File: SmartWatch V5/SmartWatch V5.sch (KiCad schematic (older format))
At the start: 61 parts, among them J1 10118192-0001LF, J10 TestPad, J2 , J8 TestPad, J9 TestPad, Q1 FDN340P, Q2 MMBT3904, Q3 MMBT3904, Q4 FDN028N20, Q5 FDN028N20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

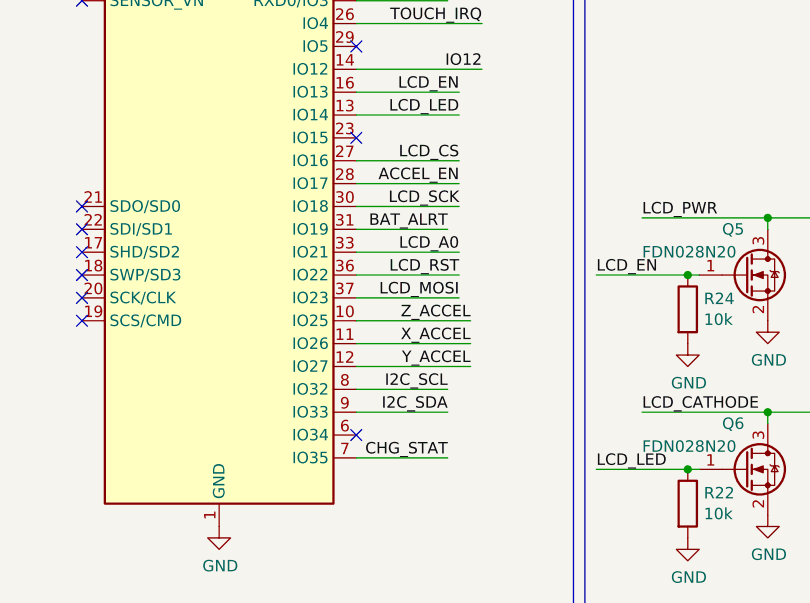
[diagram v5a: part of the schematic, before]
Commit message: Changed ACCEL_EN to IO34
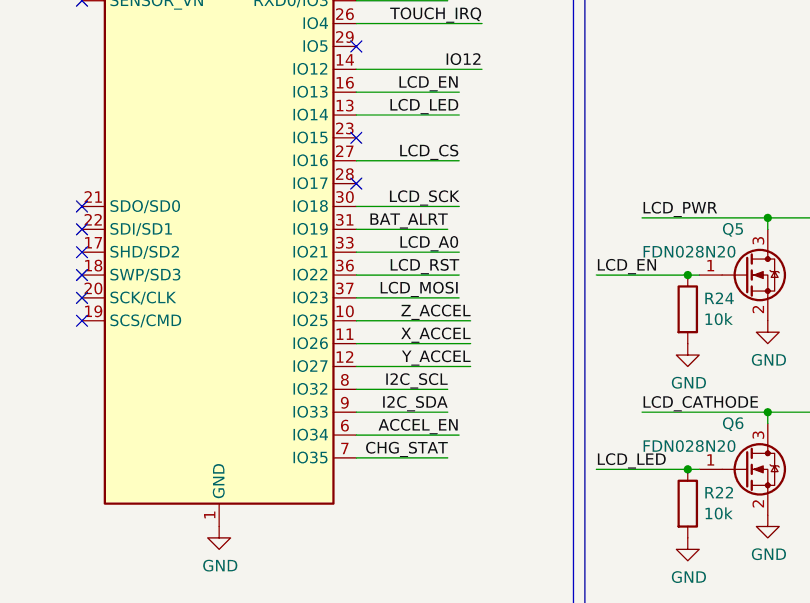
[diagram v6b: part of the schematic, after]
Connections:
- net ACCEL_EN: now also U6.6 (IO34); no longer U6.28 (IO17)
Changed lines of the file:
@@
 LCD_CS
-Wire Wire Line
-	7950 3150 8450 3150
 Wire Wire Line
 	7950 3250 8450 3250
@@
 	1    0    0    -1
 $EndComp
-Text Label 8450 3150 2    50   ~ 0
-Z_ACCEL
 Text Label 8450 3250 2    50   ~ 0
 X_ACCEL
@@
 Wire Wire Line
 	4300 2550 4650 2550
-Text Label 8400 2550 2    50   ~ 0
-ACCEL_EN
-Wire Wire Line
-	7950 2550 8400 2550
 $Comp
 L RF_Module:ESP32-WROOM-32 U6
@@
 Text Label 8350 2750 2    50   ~ 0
 BAT_ALRT
-NoConn ~ 7950 3650
 $Comp
 L power:+3.3V #PWR0129
@@
 Wire Wire Line
 	3150 1300 3600 1300
+Text Label 8450 3150 2    50   ~ 0
+Z_ACCEL
+Wire Wire Line
+	7950 3150 8450 3150
+Text Label 8400 3650 2    50   ~ 0
+ACCEL_EN
+Wire Wire Line
+	7950 3650 8400 3650
+NoConn ~ 7950 2550
 $EndSCHEMATC

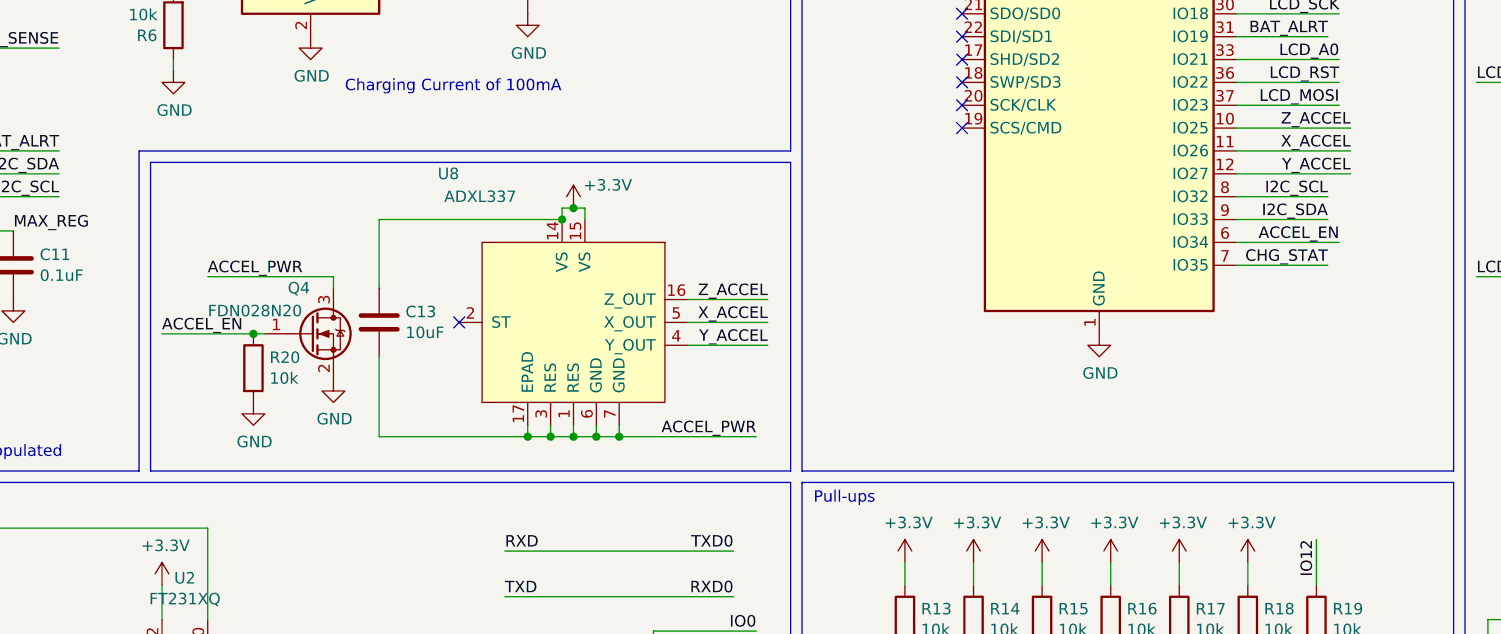
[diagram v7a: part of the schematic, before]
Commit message: Changed V5 schematic to remove enable mosfet from accelerometer
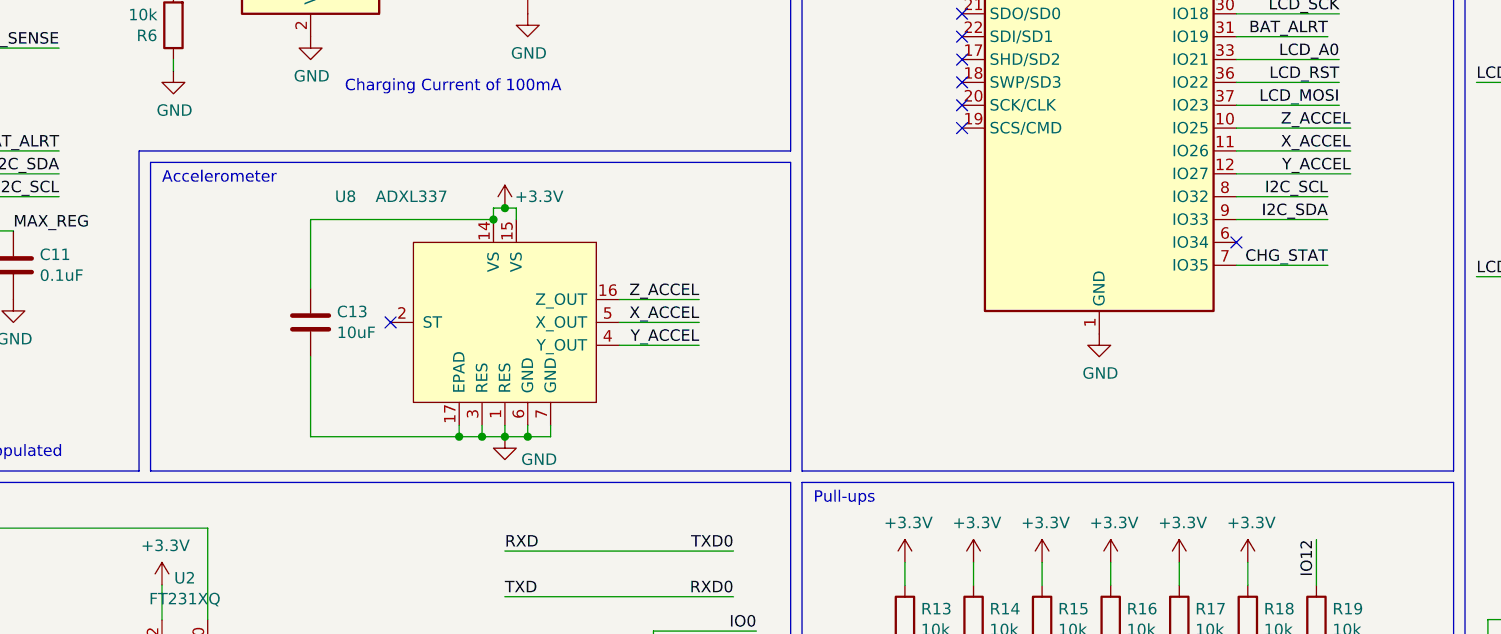
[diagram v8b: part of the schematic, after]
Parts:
- removed Q4: FDN028N20, Package_TO_SOT_SMD:SOT-23, symbol Device:Q_NMOS_GSD
- removed R20: 10k, Resistor_SMD:R_0603_1608Metric, symbol Device:R
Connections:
- net ACCEL_PWR is gone; now on net GND: C13.2, U8.1 (RES), U8.17 (EPAD), U8.3 (RES), U8.6 (GND), U8.7 (GND)
- net ACCEL_EN: no longer names the net of U6.6 (IO34)
- no-connect marks 28 -> 29
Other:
- note added: "Accelerometer\n"
- moved on the sheet: C13, U8
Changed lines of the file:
@@
 L power:+3.3V #PWR0133
 U 1 1 5F663FDD
-P 5050 3500
-F 0 "#PWR0133" H 5050 3350 50  0001 C CNN
-F 1 "+3.3V" H 5200 3600 50  0000 C CNN
-F 2 "" H 5050 3500 50  0001 C CNN
-F 3 "" H 5050 3500 50  0001 C CNN
-	1    5050 3500
-	1    0    0    -1
-$EndComp
-Wire Wire Line
-	5000 3550 5000 3500
-Wire Wire Line
-	5000 3500 5050 3500
-Wire Wire Line
-	5100 3500 5100 3550
-Connection ~ 5050 3500
-Wire Wire Line
-	5050 3500 5100 3500
+P 4750 3500
+F 0 "#PWR0133" H 4750 3350 50  0001 C CNN
+F 1 "+3.3V" H 4900 3550 50  0000 C CNN
+F 2 "" H 4750 3500 50  0001 C CNN
+F 3 "" H 4750 3500 50  0001 C CNN
+	1    4750 3500
+	1    0    0    -1
+$EndComp
+Wire Wire Line
+	4700 3550 4700 3500
+Wire Wire Line
+	4700 3500 4750 3500
+Wire Wire Line
+	4800 3500 4800 3550
+Connection ~ 4750 3500
+Wire Wire Line
+	4750 3500 4800 3500
+Wire Wire Line
+	4550 4450 4550 4500
+Wire Wire Line
+	4550 4500 4650 4500
+Wire Wire Line
+	4950 4500 4950 4450
 Wire Wire Line
 	4850 4450 4850 4500
+Connection ~ 4850 4500
 Wire Wire Line
 	4850 4500 4950 4500
 Wire Wire Line
-	5250 4500 5250 4450
-Wire Wire Line
-	5150 4450 5150 4500
-Connection ~ 5150 4500
-Wire Wire Line
-	5150 4500 5250 4500
-Wire Wire Line
-	5050 4450 5050 4500
-Connection ~ 5050 4500
-Wire Wire Line
-	5050 4500 5150 4500
-Wire Wire Line
-	4950 4450 4950 4500
-Connection ~ 4950 4500
-Wire Wire Line
-	4950 4500 5050 4500
-NoConn ~ 4550 4000
-Text Label 5900 3900 2    50   ~ 0
+	4750 4450 4750 4500
+Connection ~ 4750 4500
+Wire Wire Line
+	4750 4500 4850 4500
+Wire Wire Line
+	4650 4450 4650 4500
+Connection ~ 4650 4500
+Wire Wire Line
+	4650 4500 4750 4500
+NoConn ~ 4250 4000
+Text Label 5600 3900 2    50   ~ 0
 Z_ACCEL
-Text Label 5900 4000 2    50   ~ 0
+Text Label 5600 4000 2    50   ~ 0
 X_ACCEL
-Text Label 5900 4100 2    50   ~ 0
+Text Label 5600 4100 2    50   ~ 0
 Y_ACCEL
 Wire Wire Line
-	5900 3900 5550 3900
-Wire Wire Line
-	5900 4000 5550 4000
-Wire Wire Line
-	5900 4100 5550 4100
+	5600 3900 5250 3900
+Wire Wire Line
+	5600 4000 5250 4000
+Wire Wire Line
+	5600 4100 5250 4100
 $Comp
 L CustomParts:ADXL337 U8
 U 1 1 5F663623
-P 5050 4000
-F 0 "U8" H 4550 4650 50  0000 R CNN
-F 1 "ADXL337" H 4800 4550 50  0000 R CNN
-F 2 "CustomFootprints:ADXL337BCPZ-RL" H 4600 4450 50  0001 C CNN
-F 3 "https://www.analog.com/media/en/technical-documentation/data-sheets/ADXL337.pdf" H 4600 4450 50  0001 C CNN
-F 4 "ADXL337BCPZ-RLCT-ND" H 5050 4000 50  0001 C CNN "digikey"
-	1    5050 4000
+P 4750 4000
+F 0 "U8" H 4100 4550 50  0000 R CNN
+F 1 "ADXL337" H 4500 4550 50  0000 R CNN
+F 2 "CustomFootprints:ADXL337BCPZ-RL" H 4300 4450 50  0001 C CNN
+F 3 "https://www.analog.com/media/en/technical-documentation/data-sheets/ADXL337.pdf" H 4300 4450 50  0001 C CNN
+F 4 "ADXL337BCPZ-RLCT-ND" H 4750 4000 50  0001 C CNN "digikey"
+	1    4750 4000
 	1    0    0    -1
 $EndComp
@@
 Text Label 10700 3450 1    50   ~ 0
 LCD_PWR
-$Comp
-L Device:R R20
-U 1 1 5F503F15
-P 3650 4200
-F 0 "R20" H 3720 4246 50  0000 L CNN
-F 1 "10k" H 3720 4155 50  0000 L CNN
-F 2 "Resistor_SMD:R_0603_1608Metric" V 3580 4200 50  0001 C CNN
-F 3 "~" H 3650 4200 50  0001 C CNN
-F 4 "311-10.0KCRCT-ND" H 3650 4200 50  0001 C CNN "digikey"
-	1    3650 4200
-	1    0    0    -1
-$EndComp
-Text Label 3450 3800 0    50   ~ 0
-ACCEL_PWR
-Text Label 3250 4050 0    50   ~ 0
-ACCEL_EN
-$Comp
-L power:GND #PWR05
-U 1 1 5F503F24
-P 4000 4250
-F 0 "#PWR05" H 4000 4000 50  0001 C CNN
-F 1 "GND" H 4005 4077 50  0000 C CNN
-F 2 "" H 4000 4250 50  0001 C CNN
-F 3 "" H 4000 4250 50  0001 C CNN
-	1    4000 4250
-	1    0    0    -1
-$EndComp
-$Comp
-L power:GND #PWR04
-U 1 1 5F503F2A
-P 3650 4350
-F 0 "#PWR04" H 3650 4100 50  0001 C CNN
-F 1 "GND" H 3655 4177 50  0000 C CNN
-F 2 "" H 3650 4350 50  0001 C CNN
-F 3 "" H 3650 4350 50  0001 C CNN
-	1    3650 4350
-	1    0    0    -1
-$EndComp
-Connection ~ 3650 4050
-Wire Wire Line
-	3650 4050 3700 4050
-Wire Wire Line
-	4000 3850 4000 3800
-Wire Wire Line
-	3450 3800 4000 3800
-Wire Wire Line
-	5250 4500 5850 4500
-Connection ~ 5250 4500
-Text Label 5850 4500 2    50   ~ 0
-ACCEL_PWR
 Wire Bus Line
 	3200 3300 3200 4650
@@
 $EndComp
 $Comp
-L Device:Q_NMOS_GSD Q4
-U 1 1 5F89D454
-P 3900 4050
-F 0 "Q4" H 3800 4250 50  0000 L CNN
-F 1 "FDN028N20" H 3450 4150 50  0000 L CNN
-F 2 "Package_TO_SOT_SMD:SOT-23" H 4100 4150 50  0001 C CNN
-F 3 "https://www.onsemi.com/pub/Collateral/FDN028N20-D.pdf" H 3900 4050 50  0001 C CNN
-F 4 "FDN028N20OSCT-ND" H 3900 4050 50  0001 C CNN "digikey"
-	1    3900 4050
-	1    0    0    -1
-$EndComp
-$Comp
 L Device:R R6
 U 1 1 5E945369
@@
 	4750 5200 5750 5200
 Wire Wire Line
-	3250 4050 3650 4050
-Wire Wire Line
 	4300 2550 4650 2550
 $Comp
@@
 L Device:C C13
 U 1 1 5F57BD73
-P 4200 4000
-F 0 "C13" H 4315 4046 50  0000 L CNN
-F 1 "10uF" H 4315 3955 50  0000 L CNN
-F 2 "Capacitor_SMD:C_0603_1608Metric" H 4238 3850 50  0001 C CNN
-F 3 "~" H 4200 4000 50  0001 C CNN
-F 4 "478-10766-1-ND" H 4200 4000 50  0001 C CNN "digikey"
-	1    4200 4000
-	1    0    0    -1
-$EndComp
-Wire Wire Line
-	5000 3550 4200 3550
-Wire Wire Line
-	4200 3550 4200 3850
-Connection ~ 5000 3550
-Wire Wire Line
-	4200 4150 4200 4500
-Wire Wire Line
-	4200 4500 4850 4500
-Connection ~ 4850 4500
+P 3900 4000
+F 0 "C13" H 4015 4046 50  0000 L CNN
+F 1 "10uF" H 4015 3955 50  0000 L CNN
+F 2 "Capacitor_SMD:C_0603_1608Metric" H 3938 3850 50  0001 C CNN
+F 3 "~" H 3900 4000 50  0001 C CNN
+F 4 "478-10766-1-ND" H 3900 4000 50  0001 C CNN "digikey"
+	1    3900 4000
+	1    0    0    -1
+$EndComp
+Wire Wire Line
+	4700 3550 3900 3550
+Wire Wire Line
+	3900 3550 3900 3850
+Connection ~ 4700 3550
+Wire Wire Line
+	3900 4150 3900 4500
+Wire Wire Line
+	3900 4500 4550 4500
+Connection ~ 4550 4500
 $Comp
 L Device:C C15
@@
 Wire Wire Line
 	7950 3150 8450 3150
-Text Label 8400 3650 2    50   ~ 0
-ACCEL_EN
-Wire Wire Line
-	7950 3650 8400 3650
 NoConn ~ 7950 2550
 $Comp
@@
 	0    1    1    0
 $EndComp
+$Comp
+L power:GND #PWR?
+U 1 1 601347E9
+P 4750 4500
+F 0 "#PWR?" H 4750 4250 50  0001 C CNN
+F 1 "GND" H 4900 4400 50  0000 C CNN
+F 2 "" H 4750 4500 50  0001 C CNN
+F 3 "" H 4750 4500 50  0001 C CNN
+	1    4750 4500
+	1    0    0    -1
+$EndComp
+Text Notes 3250 3400 0    50   ~ 0
+Accelerometer\n
+NoConn ~ 7950 3650
 $EndSCHEMATC
